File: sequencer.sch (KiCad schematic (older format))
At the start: 190 parts, among them IC1 ATMEGA328PB, IC2 AT24CS64-XHM, SW10 INST_CH_12, SW11 SHIFT, SW12 IF_VAR, SW13 INST_LT_4, SW14 INST_MT_5, SW15 INST_HT_6, SW16 INST_RS_7, SW17 INST_CP_8, SW18 INST_CB_9, SW19 INST_CY_10, SW2 BASIC_VAR_A, SW20 INST_OH_11, SW21 START/STOP, SW22 TAP, SW3 BASIC_VAR_B, SW4 MODE, SW5 FILL, SW6 CLEAR, SW7 INST_AC_1, SW8 INST_BD_2, SW9 INST_SD_3, U27 74HC165, U28 74HC165, U29 74HC165, U30 74AC595, U31 74AC595, U32 74AC595, U33 74AC595, U34 74AC595, U35 R-78E5.0-1.0, U36 74AC595, U37 74AC595, X1 MIDI IN, Y1 16MHz

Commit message: assigning footprints before importing updated netlist into pcbnew
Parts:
- D75: renamed from D?; footprint (none) -> Pin_Headers:Pin_Header_Straight_1x03_Pitch2.00mm
- P3: renamed from P?; footprint (none) -> Pin_Headers:Pin_Header_Straight_2x06
- SW10, SW13, SW14, SW15, SW16, SW17, SW18, SW19, SW20, SW7, SW8, SW9: footprint MyModules:KS-01Q-02-SPST -> MyModules:B3F-1050-OMRON
- SW11, SW4, SW5: footprint MyModules:KS-01Q-02-SPST -> MyModules:BF-4050-PCB-ADAPT
- gave numbers to parts that had none: 14

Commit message: surface mount polarized capacitors replace through hole capaictors. Updated netlist not yet imported into pcbnew
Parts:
- C188, C189: footprint MyModules:2MM-POL-CAP -> Capacitors_SMD:c_elec_4x5.3
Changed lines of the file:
@@
 F 0 "C189" H 18325 4050 50  0000 L CNN
 F 1 "10µF" H 18325 3850 50  0000 L CNN
-F 2 "MyModules:2MM-POL-CAP" H 18275 3950 60  0001 C CNN
+F 2 "Capacitors_SMD:c_elec_4x5.3" H 18275 3950 60  0001 C CNN
 F 3 "~" H 18275 3950 60  0000 C CNN
 	1    18275 3950
@@
 F 0 "C188" H 17225 4050 50  0000 L CNN
 F 1 " 10µ" H 17225 3850 50  0000 L CNN
-F 2 "MyModules:2MM-POL-CAP" H 17175 3950 60  0001 C CNN
+F 2 "Capacitors_SMD:c_elec_4x5.3" H 17175 3950 60  0001 C CNN
 F 3 "~" H 17175 3950 60  0000 C CNN
 	1    17175 3950

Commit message: changed trigger connectors to 3 x 6 position JST GH series, pending cable assembly availabilty. Commit before importing netlist
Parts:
- added P5: CONN_02X03, MyModules:GH-TOP-6, symbol CONN_02X03
- P3: footprint Pin_Headers:Pin_Header_Straight_2x06 -> MyModules:GH-TOP-6; symbol CONN_02X06 -> CONN_02X03
- P4: footprint synth:CONN-2X3-0100R -> MyModules:GH-TOP-6
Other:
- note added: "TRIGGER \nHEADERS"
- note removed: "TRIGGER \nHEADER"
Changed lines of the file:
@@
 DIN RESET PIN \nCONNECTED\nBUT ALSO USED\nTO DRIVE YELLOW\nSYNC LED
 $Comp
-L CONN_02X06 P3
+L CONN_02X03 P3
 U 1 1 57DD315C
-P 11125 9225
+P 11125 9375
 F 0 "P3" H 11125 9575 50  0000 C CNN
-F 1 "CONN_02X06" H 11125 8875 50  0000 C CNN
-F 2 "Pin_Headers:Pin_Header_Straight_2x06" H 11125 8025 60  0001 C CNN
-F 3 "" H 11125 8025 60  0000 C CNN
-	1    11125 9225
+F 1 "CONN_02X06" H 11125 9025 50  0000 C CNN
+F 2 "MyModules:GH-TOP-6" H 11125 8175 60  0001 C CNN
+F 3 "" H 11125 8175 60  0000 C CNN
+	1    11125 9375
 	1    0    0    -1
 $EndComp
-Text HLabel 10875 8975 0    50   Output ~ 0
+Text HLabel 9450 9225 0    50   Output ~ 0
 ACCENT
-Text HLabel 11375 8975 2    50   Output ~ 0
+Text HLabel 9950 9225 2    50   Output ~ 0
 BD_TRIG
-Text HLabel 10875 9075 0    50   Output ~ 0
+Text HLabel 9450 9325 0    50   Output ~ 0
 SD_TRIG
-Text HLabel 11375 9075 2    50   Output ~ 0
+Text HLabel 9950 9325 2    50   Output ~ 0
 LT_TRIG
-Text HLabel 10875 9175 0    50   Output ~ 0
+Text HLabel 9450 9425 0    50   Output ~ 0
 MT_TRIG
-Text HLabel 11375 9175 2    50   Output ~ 0
+Text HLabel 9950 9425 2    50   Output ~ 0
 HT_TRIG
 Text HLabel 10875 9275 0    50   Output ~ 0
@@
 CP_TRIG
 Text Notes 10950 8825 0    60   ~ 0
-TRIGGER \nHEADER
+TRIGGER \nHEADERS
 $Comp
 L GND_E #PWR0490
@@
 F 0 "P4" H 11350 10425 50  0000 C CNN
 F 1 "CONN_02X03" H 11350 10025 50  0000 C CNN
-F 2 "synth:CONN-2X3-0100R" H 11350 9025 60  0001 C CNN
+F 2 "MyModules:GH-TOP-6" H 11350 9025 60  0001 C CNN
 F 3 "" H 11350 9025 60  0000 C CNN
 	1    11350 10225
@@
 Wire Wire Line
 	11675 10325 11675 10500
+$Comp
+L CONN_02X03 P5
+U 1 1 57B54F0F
+P 9700 9325
+F 0 "P5" H 9700 9525 50  0000 C CNN
+F 1 "CONN_02X03" H 9700 9125 50  0000 C CNN
+F 2 "MyModules:GH-TOP-6" H 9700 8125 60  0001 C CNN
+F 3 "" H 9700 8125 60  0000 C CNN
+	1    9700 9325
+	1    0    0    -1
+$EndComp
 $EndSCHEMATC

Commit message: reconfigured trigger connectors and routed. Now just power and ground left
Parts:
- P3: value CONN_02X06 -> CONN_02X02; footprint MyModules:GH-TOP-6 -> MyModules:GH-TOP-4; symbol CONN_02X03 -> CONN_02X02
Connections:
- net +5V: now also P4.5 (P5); no longer P3.3 (P3), P3.4 (P4)
- net CB_TRIG: now also P4.1 (P1); no longer P4.2 (P2)
- net CH_TRIG: now also P4.4 (P4); no longer P4.5 (P5)
- net CY_TRIG: now also P4.2 (P2); no longer P4.3 (P3)
- net GND: now also P3.4 (P4); no longer P3.5 (P5), P3.6 (P6)
- net MA_TRIG: now also P3.3 (P3); no longer P4.1 (P1)
- net OH_TRIG: now also P4.3 (P3); no longer P4.4 (P4)
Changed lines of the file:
@@
 DIN RESET PIN \nCONNECTED\nBUT ALSO USED\nTO DRIVE YELLOW\nSYNC LED
 $Comp
-L CONN_02X03 P3
+L CONN_02X02 P3
 U 1 1 57DD315C
-P 11125 9375
-F 0 "P3" H 11125 9575 50  0000 C CNN
-F 1 "CONN_02X06" H 11125 9025 50  0000 C CNN
-F 2 "MyModules:GH-TOP-6" H 11125 8175 60  0001 C CNN
-F 3 "" H 11125 8175 60  0000 C CNN
-	1    11125 9375
+P 11125 9325
+F 0 "P3" H 11125 9525 50  0000 C CNN
+F 1 "CONN_02X02" H 11125 9175 50  0000 C CNN
+F 2 "MyModules:GH-TOP-4" H 11125 8125 60  0001 C CNN
+F 3 "" H 11125 8125 60  0000 C CNN
+	1    11125 9325
 	1    0    0    -1
 $EndComp
@@
 L GND_E #PWR0490
 U 1 1 57DD8A3A
-P 11475 9625
-F 0 "#PWR0490" V 11475 9625 30  0001 C CNN
-F 1 "GND_E" H 11475 9555 30  0001 C CNN
-F 2 "~" H 11475 9625 60  0000 C CNN
-F 3 "~" H 11475 9625 60  0000 C CNN
-	1    11475 9625
+P 11475 9525
+F 0 "#PWR0490" V 11475 9525 30  0001 C CNN
+F 1 "GND_E" H 11475 9455 30  0001 C CNN
+F 2 "~" H 11475 9525 60  0000 C CNN
+F 3 "~" H 11475 9525 60  0000 C CNN
+	1    11475 9525
 	1    0    0    -1
 $EndComp
 Wire Wire Line
-	11375 9475 11475 9475
+	11375 9375 11475 9375
 Wire Wire Line
-	11475 9475 11475 9625
-$Comp
-L GND_E #PWR0491
-U 1 1 57DD9779
-P 10775 9625
-F 0 "#PWR0491" V 10775 9625 30  0001 C CNN
-F 1 "GND_E" H 10775 9555 30  0001 C CNN
-F 2 "~" H 10775 9625 60  0000 C CNN
-F 3 "~" H 10775 9625 60  0000 C CNN
-	1    10775 9625
-	1    0    0    -1
-$EndComp
-Wire Wire Line
-	10875 9475 10775 9475
-Wire Wire Line
-	10775 9475 10775 9625
-$Comp
-L 5V #PWR0492
-U 1 1 57DDA1C6
-P 11875 9325
-F 0 "#PWR0492" H 11875 9175 50  0001 C CNN
-F 1 "5V" H 11875 9500 50  0000 C CNN
-F 2 "" H 11875 9325 60  0000 C CNN
-F 3 "" H 11875 9325 60  0000 C CNN
-	1    11875 9325
-	1    0    0    -1
-$EndComp
-Wire Wire Line
-	11375 9375 11875 9375
-Wire Wire Line
-	11875 9375 11875 9325
+	11475 9375 11475 9525
 $Comp
 L 5V #PWR0493
 U 1 1 57DDA864
-P 10375 9325
-F 0 "#PWR0493" H 10375 9175 50  0001 C CNN
-F 1 "5V" H 10375 9500 50  0000 C CNN
-F 2 "" H 10375 9325 60  0000 C CNN
-F 3 "" H 10375 9325 60  0000 C CNN
-	1    10375 9325
+P 10675 10050
+F 0 "#PWR0493" H 10675 9900 50  0001 C CNN
+F 1 "5V" H 10675 10225 50  0000 C CNN
+F 2 "" H 10675 10050 60  0000 C CNN
+F 3 "" H 10675 10050 60  0000 C CNN
+	1    10675 10050
 	1    0    0    -1
 $EndComp
-Wire Wire Line
-	10375 9325 10375 9375
-Wire Wire Line
-	10375 9375 10875 9375
 $Comp
 L CONN_02X03 P4
@@
 	1    0    0    -1
 $EndComp
+Text HLabel 10875 9375 0    50   Output ~ 0
+MA_TRIG
 Text HLabel 11100 10125 0    50   Output ~ 0
-MA_TRIG
+CB_TRIG
 Text HLabel 11600 10125 2    50   Output ~ 0
-CB_TRIG
+CY_TRIG
 Text HLabel 11100 10225 0    50   Output ~ 0
-CY_TRIG
+OH_TRIG
 Text HLabel 11600 10225 2    50   Output ~ 0
-OH_TRIG
-Text HLabel 11100 10325 0    50   Output ~ 0
 CH_TRIG
 $Comp
@@
 	1    0    0    -1
 $EndComp
+Wire Wire Line
+	10675 10050 10675 10325
+Wire Wire Line
+	10675 10325 11100 10325
 $EndSCHEMATC

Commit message: removed SW3 from schematic and PCB. more fiddling with panel mounting screws
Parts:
- removed R386: 10K, MyModules:SM0603-R-JRL, symbol R_US
- removed SW3: BASIC_VAR_B, MyModules:B3F-1050-OMRON, symbol TACT_SWITCH
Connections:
- no-connect marks 15 -> 16
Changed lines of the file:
@@
 $EndComp
 $Comp
-L R_US R386
-U 1 1 56AB4403
-P 3400 6550
-F 0 "R386" V 3450 6700 50  0000 C CNN
-F 1 "10K" V 3320 6550 50  0000 C CNN
-F 2 "MyModules:SM0603-R-JRL" H 3400 6550 60  0001 C CNN
-F 3 "~" H 3400 6550 60  0000 C CNN
-	1    3400 6550
-	-1   0    0    1
-$EndComp
-$Comp
-L GND_E #PWR0416
-U 1 1 56AB440A
-P 3400 6800
-F 0 "#PWR0416" V 3400 6800 30  0001 C CNN
-F 1 "GND_E" H 3400 6730 30  0001 C CNN
-F 2 "~" H 3400 6800 60  0000 C CNN
-F 3 "~" H 3400 6800 60  0000 C CNN
-	1    3400 6800
-	1    0    0    -1
-$EndComp
-$Comp
 L R_US R387
 U 1 1 56AB4410
@@
 	1950 9400 1950 9500
 Wire Wire Line
-	3050 6300 3050 8000
-Wire Wire Line
-	3050 8000 2650 8000
-Wire Wire Line
 	3100 7100 3100 8100
 Wire Wire Line
@@
 	3400 5950 3400 6000
 Wire Wire Line
-	3400 6300 3400 6350
-Wire Wire Line
-	3400 6750 3400 6800
-Wire Wire Line
 	3400 7100 3400 7150
 Wire Wire Line
@@
 Wire Wire Line
 	1250 9400 1950 9400
-Connection ~ 3400 6300
 Connection ~ 3400 7100
 Connection ~ 3400 7900
@@
 	3000 5500 3775 5500
 Wire Wire Line
-	3050 6300 3775 6300
-Wire Wire Line
 	3100 7100 3775 7100
 Wire Wire Line
@@
 Connection ~ 4275 8700
 Connection ~ 4275 7100
-Connection ~ 4275 6300
 Connection ~ 4275 5500
 Wire Wire Line
@@
 Text GLabel 12700 3375 2    50   Input ~ 0
 SYNC_IN
-$Comp
-L TACT_SWITCH SW3
-U 1 1 56BB5434
-P 4025 6300
-F 0 "SW3" V 4175 6525 50  0000 C CNN
-F 1 "BASIC_VAR_B" V 3925 6300 50  0000 C CNN
-F 2 "MyModules:B3F-1050-OMRON" H 4025 6150 60  0001 C CNN
-F 3 "" H 4025 6150 60  0000 C CNN
-	1    4025 6300
-	0    -1   -1   0
-$EndComp
 Text Notes 4325 6400 0    50   ~ 0
 SW3 BASIC VAR B \nneeds to be deleted
@@
 	11475 9375 11475 9525
 $Comp
-L 5V #PWR0493
+L 5V #PWR0491
 U 1 1 57DDA864
 P 10675 10050
-F 0 "#PWR0493" H 10675 9900 50  0001 C CNN
+F 0 "#PWR0491" H 10675 9900 50  0001 C CNN
 F 1 "5V" H 10675 10225 50  0000 C CNN
 F 2 "" H 10675 10050 60  0000 C CNN
@@
 CH_TRIG
 $Comp
-L GND_E #PWR0494
+L GND_E #PWR0492
 U 1 1 57DE40B4
 P 11675 10500
-F 0 "#PWR0494" V 11675 10500 30  0001 C CNN
+F 0 "#PWR0492" V 11675 10500 30  0001 C CNN
 F 1 "GND_E" H 11675 10430 30  0001 C CNN
 F 2 "~" H 11675 10500 60  0000 C CNN
@@
 Wire Wire Line
 	10675 10325 11100 10325
+NoConn ~ 2650 8000
 $EndSCHEMATC

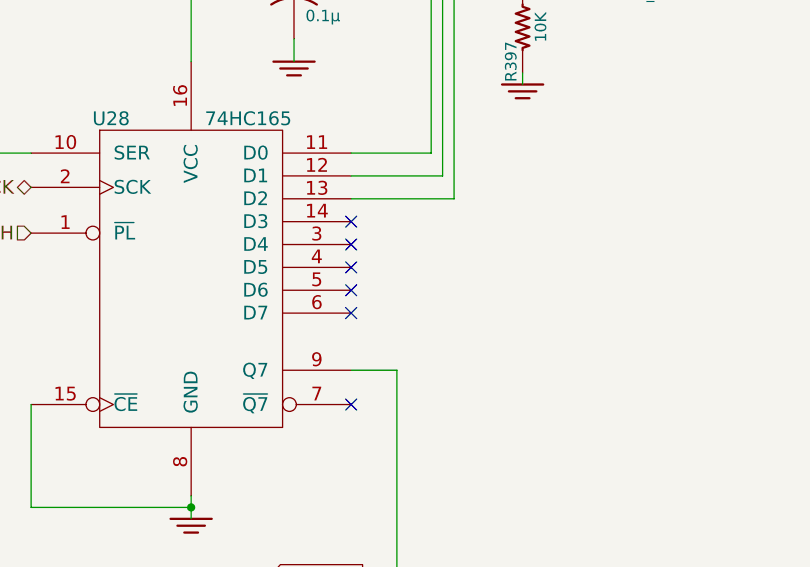
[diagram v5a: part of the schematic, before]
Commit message: ground plane now split into analog and digital regions. More stitching required and then need to decide how to link them up. Also, schematic has U28 unused inputs now grounded as these were oscillating spuriously. Still need to import updated netlist into pcbnew. If all goes to heck, go back to previous commit
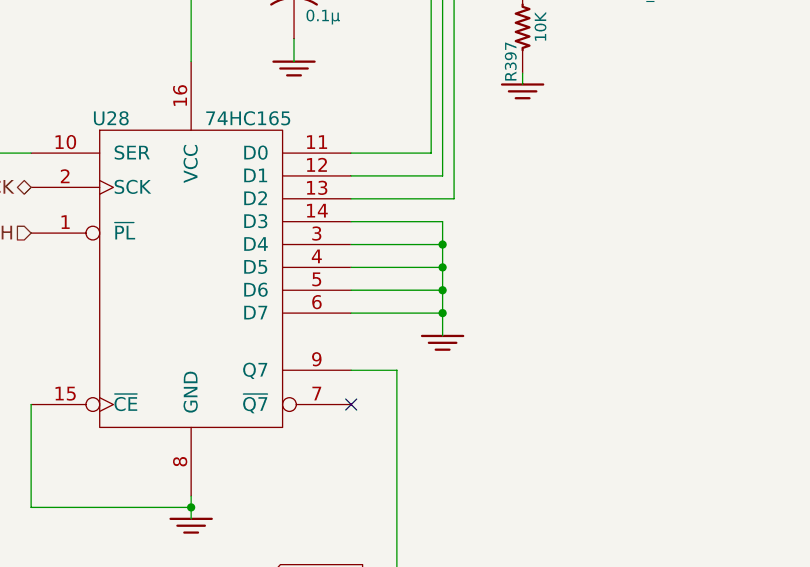
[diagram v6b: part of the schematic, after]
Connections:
- net GND: now also U28.14 (D3), U28.3 (D4), U28.4 (D5), U28.5 (D6), U28.6 (D7)
- no-connect marks 16 -> 11

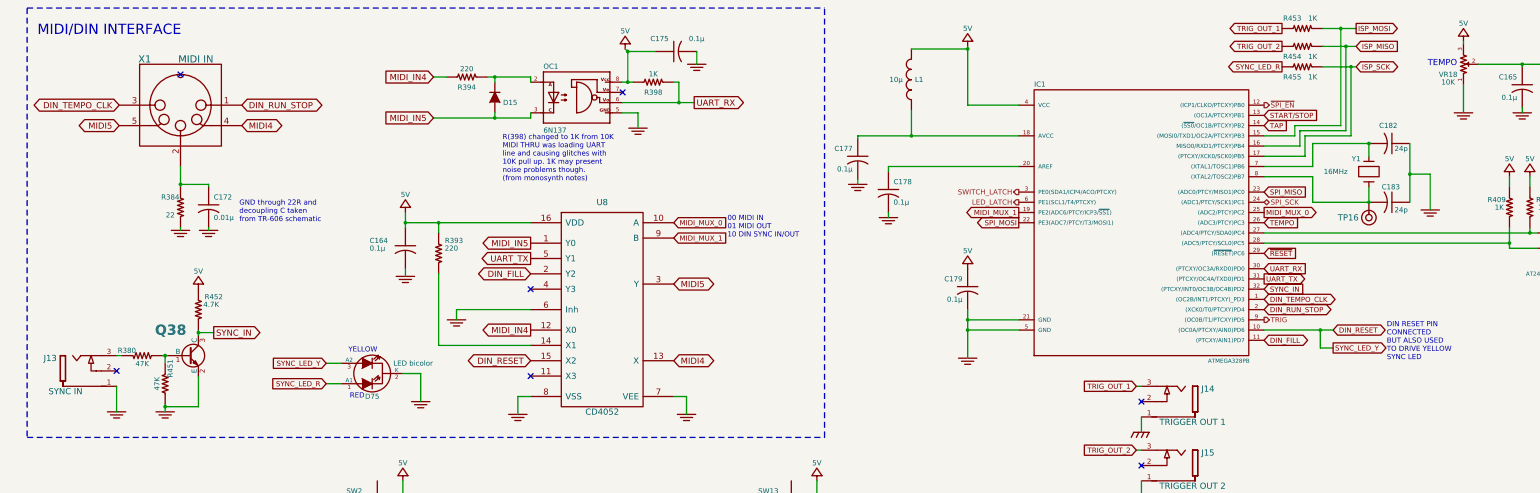
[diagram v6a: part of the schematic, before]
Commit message: changed MIDI circuitry. supports DIN SYNC IN/OUT and MIDI IN, no out. MIDI TX and remaining DIN lines broken out to 4 pin JST GH connector
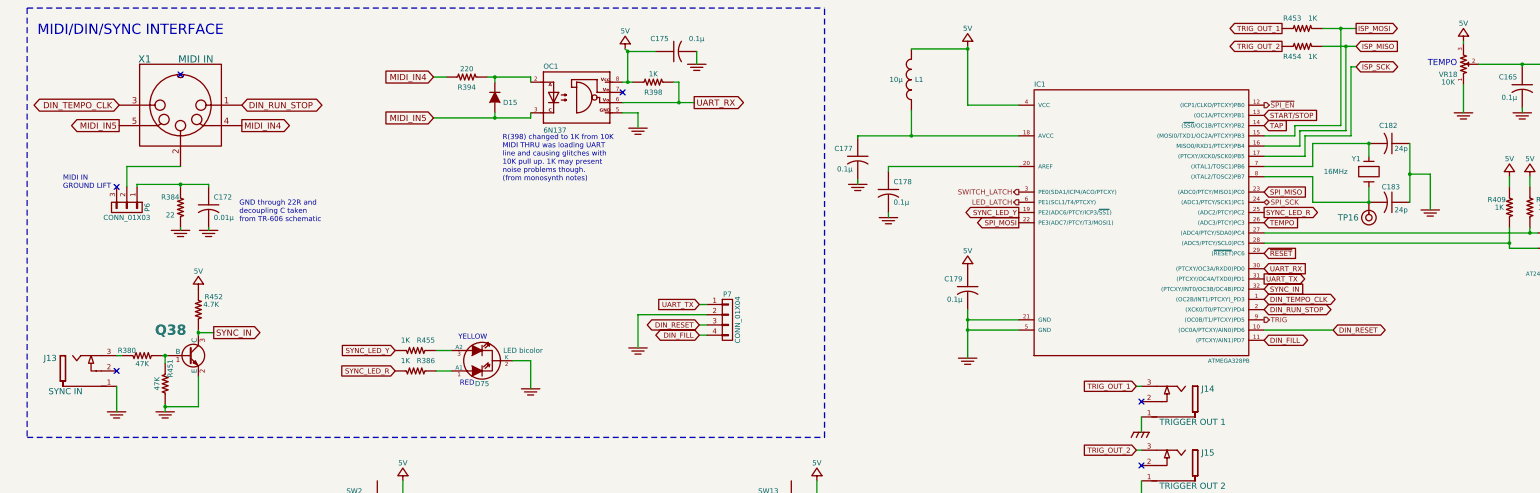
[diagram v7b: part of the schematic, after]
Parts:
- removed C164: 0.1µ, MyModules:SM0603-C-JRL, symbol C_US
- removed R393: 220, MyModules:SM0603-R-JRL, symbol R_US
- removed U8: CD4052, Housings_SSOP:TSSOP-16_4.4x5mm_Pitch0.65mm, symbol CD4052
- added P6: CONN_01X03, Pin_Headers:Pin_Header_Straight_1x03, symbol CONN_01X03
- added P7: CONN_01X04, MyModules:GH-TOP-4, symbol CONN_01X04
- added R386: 1K, MyModules:SM0603-R-JRL, symbol R_US
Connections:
- net MIDI4 is gone; now on net MIDI_IN4: X1.4
- net MIDI5 is gone; now on net MIDI_IN5: X1.5
- net MIDI_MUX_0 is gone; now on net SYNC_LED_R: IC1.25 ((ADC2/PTCY)PC2)
- net DIN_FILL: now also P7.4 (P4)
- net DIN_RESET: now also P7.3 (P3); no longer D75.3 (A2)
- net GND: now also P7.2 (P2)
- net ISP_SCK: no longer R455.1
- net SYNC_LED_R: now also R386.1; no longer D75.1 (A1), R455.2
- net UART_TX: now also P7.1 (P1)
- net at C172.1, R384.2: now also P6.1 (P1); no longer X1.2
- net MIDI_MUX_1 renamed SYNC_LED_Y
- net SYNC_LED_Y: now also R455.1
- new net: P6.2 (P2), X1.2
- new net: D75.1 (A1), R386.2
- new net: D75.3 (A2), R455.2
- no-connect marks 11 -> 10
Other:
- note added: "MIDI IN\nGROUND LIFT"
- note added: "MIDI/DIN/SYNC INTERFACE"
- note removed: "00 MIDI IN\n01 MIDI OUT\n10 DIN SYNC IN/OUT"
- note removed: "DIN RESET PIN \nCONNECTED\nBUT ALSO USED\nTO DRIVE YELLOW\nSYNC LED"
- note removed: "MIDI/DIN INTERFACE"
- moved on the sheet: D75

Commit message: updated readme, changed a few things
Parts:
- R386, R455: value 1K -> 270
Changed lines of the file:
@@
 P 4400 3975
 F 0 "R455" V 4500 3875 50  0000 C CNN
-F 1 "1K" V 4500 4075 50  0000 C CNN
+F 1 "270" V 4500 4075 50  0000 C CNN
 F 2 "MyModules:SM0603-R-JRL" H 4400 3975 60  0001 C CNN
 F 3 "~" H 4400 3975 60  0000 C CNN
@@
 P 4400 4175
 F 0 "R386" V 4500 4075 50  0000 C CNN
-F 1 "1K" V 4500 4275 50  0000 C CNN
+F 1 "270" V 4500 4275 50  0000 C CNN
 F 2 "MyModules:SM0603-R-JRL" H 4400 4175 60  0001 C CNN
 F 3 "~" H 4400 4175 60  0000 C CNN
